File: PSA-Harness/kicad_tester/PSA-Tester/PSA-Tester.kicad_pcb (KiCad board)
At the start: 4 copper layers, 100 x 100 mm, 41 parts, among them J11 U262-241N-4BV60, M1 MountingHole_3.2mm_M3_Pad_Via, M2 MountingHole_3.2mm_M3_Pad_Via, M3 MountingHole_3.2mm_M3_Pad_Via, M4 MountingHole_3.2mm_M3_Pad_Via, SW1 B3S-1000, SW2 B3S-1000, SW3 B3S-1000, U1 MCP23017T-E/SO, U10 ESP32-C3-OLED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

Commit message: change usb-c type and button
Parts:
- J11: value U262-241N-4BV60 -> TYPE-C-31-M-04
- SW1, SW2, SW3: value B3S-1000 -> B3FS-1010P; footprint 0_tester:SW_SPST_B3S-1000 -> 0_tester:SW_SPST_Omron_B3FS-101xP

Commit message: fix DRC
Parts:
- moved SW2 0.26 mm to (129.0, 113.4)
- moved SW3 0.26 mm to (129.0, 127.4)
- moved SW1 0.26 mm to (129.0, 99.7)
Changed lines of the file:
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@@
 	(footprint "0_tester:SW_SPST_Omron_B3FS-101xP"
 		(layer "F.Cu")
-		(at 128.74 99.75 180)
+		(at 128.975 99.65 180)
 		(descr "Surface Mount Tactile Switch for High-Density Mounting, 4.3mm height, https://omronfs.omron.com/en_US/ecb/products/pdf/en-b3fs.pdf")
 		(tags "Tactile Switch")
@@
 	(footprint "0_tester:SW_SPST_Omron_B3FS-101xP"
 		(layer "F.Cu")
-		(at 128.765 127.5 180)
+		(at 129 127.4 180)
 		(descr "Surface Mount Tactile Switch for High-Density Mounting, 4.3mm height, https://omronfs.omron.com/en_US/ecb/products/pdf/en-b3fs.pdf")
 		(tags "Tactile Switch")
@@
 	(footprint "0_tester:SW_SPST_Omron_B3FS-101xP"
 		(layer "F.Cu")
-		(at 128.765 113.5 180)
+		(at 129 113.4 180)
 		(descr "Surface Mount Tactile Switch for High-Density Mounting, 4.3mm height, https://omronfs.omron.com/en_US/ecb/products/pdf/en-b3fs.pdf")
 		(tags "Tactile Switch")
@@
 	)
 	(segment
-		(start 124.79 115.75)
-		(end 125.8267 115.75)
-		(width 0.2)
-		(layer "F.Cu")
-		(net 145)
-	)
-	(segment
-		(start 130.55 129.558)
-		(end 131.5113 129.558)
+		(start 114.9466 81.5534)
+		(end 114.9 81.6)
 		(width 0.2)
 		(layer "F.Cu")
@@
 	)
 	(segment
-		(start 114.9466 81.5534)
-		(end 114.9 81.6)
+		(start 100.4059 107.5059)
+		(end 99.695 106.795)
 		(width 0.2)
 		(layer "F.Cu")
@@
 	)
 	(segment
-		(start 100.4059 107.5059)
-		(end 99.695 106.795)
+		(start 124.932 115.608)
+		(end 126.6 115.608)
 		(width 0.2)
 		(layer "F.Cu")
@@
 	)
 	(segment
-		(start 124.765 103.048)
-		(end 124.765 102)
-		(width 0.2)
-		(layer "F.Cu")
-		(net 145)
-	)
-	(segment
 		(start 56.9777 81.9637)
 		(end 58.1513 81.9637)
@@
 	)
 	(segment
+		(start 132.59 115.6)
+		(end 131.4 115.6)
+		(width 0.2)
+		(layer "F.Cu")
+		(net 145)
+	)
+	(segment
 		(start 99.895 108.065)
 		(end 99 108.065)
@@
 	)
 	(segment
-		(start 126.2245 129.558)
-		(end 126.0187 129.558)
-		(width 0.2)
-		(layer "F.Cu")
-		(net 145)
-	)
-	(segment
-		(start 132.994 114.386)
-		(end 132.74 114.64)
+		(start 108.554 80.427)
+		(end 109.727 80.427)
 		(width 0.2)
 		(layer "F.Cu")
@@
 	)
 	(segment
-		(start 108.554 80.427)
-		(end 109.727 80.427)
+		(start 99.229 88.394)
+		(end 99 88.165)
 		(width 0.2)
 		(layer "F.Cu")
@@
 	)
 	(segment
-		(start 99.229 88.394)
-		(end 99 88.165)
+		(start 132.715 102)
+		(end 131.4 102)
 		(width 0.2)
 		(layer "F.Cu")
@@
 	)
 	(segment
-		(start 131.5113 129.558)
-		(end 131.7033 129.75)
+		(start 124.896812 129.643188)
+		(end 126.8 129.643188)
 		(width 0.2)
 		(layer "F.Cu")
@@
 	)
 	(segment
-		(start 132.74 114.64)
-		(end 132.74 115.75)
-		(width 0.2)
-		(layer "F.Cu")
-		(net 145)
-	)
-	(segment
-		(start 124.79 129.75)
-		(end 125.8267 129.75)
+		(start 124.79 115.75)
+		(end 124.932 115.608)
 		(width 0.2)
 		(layer "F.Cu")
@@
 	)
 	(segment
+		(start 132.548 129.558)
+		(end 131.4 129.558)
+		(width 0.2)
+		(layer "F.Cu")
+		(net 145)
+	)
+	(segment
 		(start 81.3845 86.2742)
 		(end 82.0053 86.895)
@@
 	)
 	(segment
-		(start 124.99 103.273)
-		(end 124.765 103.048)
+		(start 124.79 129.75)
+		(end 124.896812 129.643188)
 		(width 0.2)
 		(layer "F.Cu")
@@
 	)
 	(segment
+		(start 132.74 129.75)
+		(end 132.548 129.558)
+		(width 0.2)
+		(layer "F.Cu")
+		(net 145)
+	)
+	(segment
 		(start 87.715 101.715)
 		(end 87.7 101.7)
@@
 	)
 	(segment
-		(start 126.0187 129.558)
-		(end 125.8267 129.75)
-		(width 0.2)
-		(layer "F.Cu")
-		(net 145)
-	)
-	(segment
 		(start 72.1344 100.9111)
 		(end 72.8983 101.675)
@@
 	)
 	(segment
-		(start 125.9687 115.608)
-		(end 125.8267 115.75)
-		(width 0.2)
-		(layer "F.Cu")
-		(net 145)
-	)
-	(segment
 		(start 100.4059 107.562)
 		(end 100.4059 107.5059)
@@
 	)
 	(segment
-		(start 132.74 129.75)
-		(end 131.7033 129.75)
-		(width 0.2)
-		(layer "F.Cu")
-		(net 145)
-	)
-	(segment
 		(start 45.01 80.6796)
 		(end 43.9546 81.735)
@@
 	)
 	(segment
+		(start 124.765 102)
+		(end 126.6 102)
+		(width 0.2)
+		(layer "F.Cu")
+		(net 145)
+	)
+	(segment
 		(start 70.44 105.54)
 		(end 70.45 105.55)
@@
 	)
 	(segment
-		(start 132.715 102.994)
-		(end 132.715 102)
-		(width 0.2)
-		(layer "F.Cu")
-		(net 145)
-	)
-	(segment
 		(start 109.727 80.427)
 		(end 110.9 81.6)
@@
 	)
 	(segment
-		(start 132.994 103.273)
-		(end 132.715 102.994)
-		(width 0.2)
-		(layer "F.Cu")
-		(net 145)
-	)
-	(segment
 		(start 56.9309 102.2612)
 		(end 56.9309 102.2591)
@@
 	)
 	(segment
-		(start 126.2245 115.608)
-		(end 125.9687 115.608)
+		(start 132.74 115.75)
+		(end 132.59 115.6)
 		(width 0.2)
 		(layer "F.Cu")
@@
 	)
 	(via
-		(at 132.994 114.386)
+		(at 131.4 115.6)
 		(size 0.5)
 		(drill 0.3)
@@
 	)
 	(via
-		(at 124.99 103.273)
+		(at 126.6 102)
 		(size 0.5)
 		(drill 0.3)
@@
 	)
 	(via
-		(at 126.2245 129.558)
+		(at 126.8 129.643188)
 		(size 0.5)
 		(drill 0.3)
@@
 	)
 	(via
-		(at 130.55 129.558)
+		(at 131.4 129.558)
 		(size 0.5)
 		(drill 0.3)
@@
 	)
 	(via
-		(at 126.2245 115.608)
+		(at 126.6 115.608)
 		(size 0.5)
 		(drill 0.3)
@@
 	)
 	(via
-		(at 132.994 103.273)
+		(at 131.4 102)
 		(size 0.5)
 		(drill 0.3)

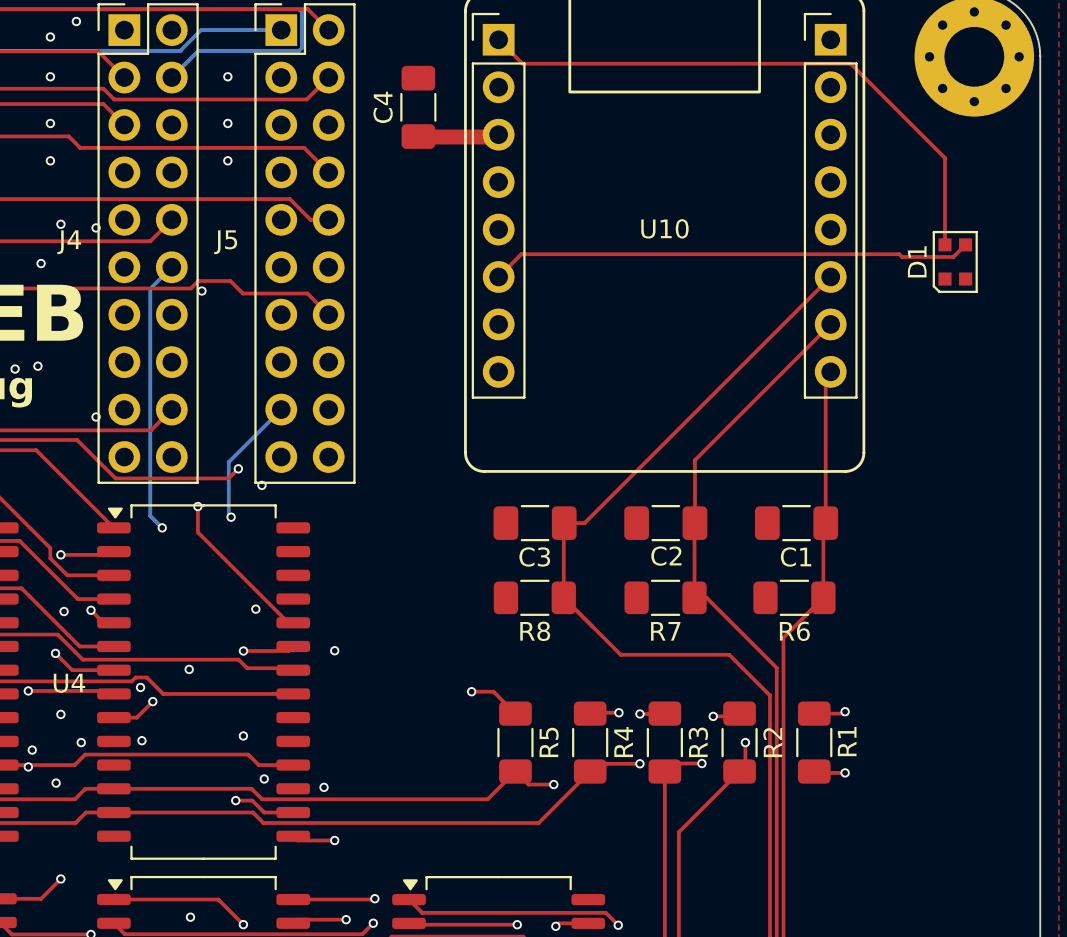
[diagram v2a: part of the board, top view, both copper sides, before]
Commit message: fix pin5/pin6 used by I2C OLED
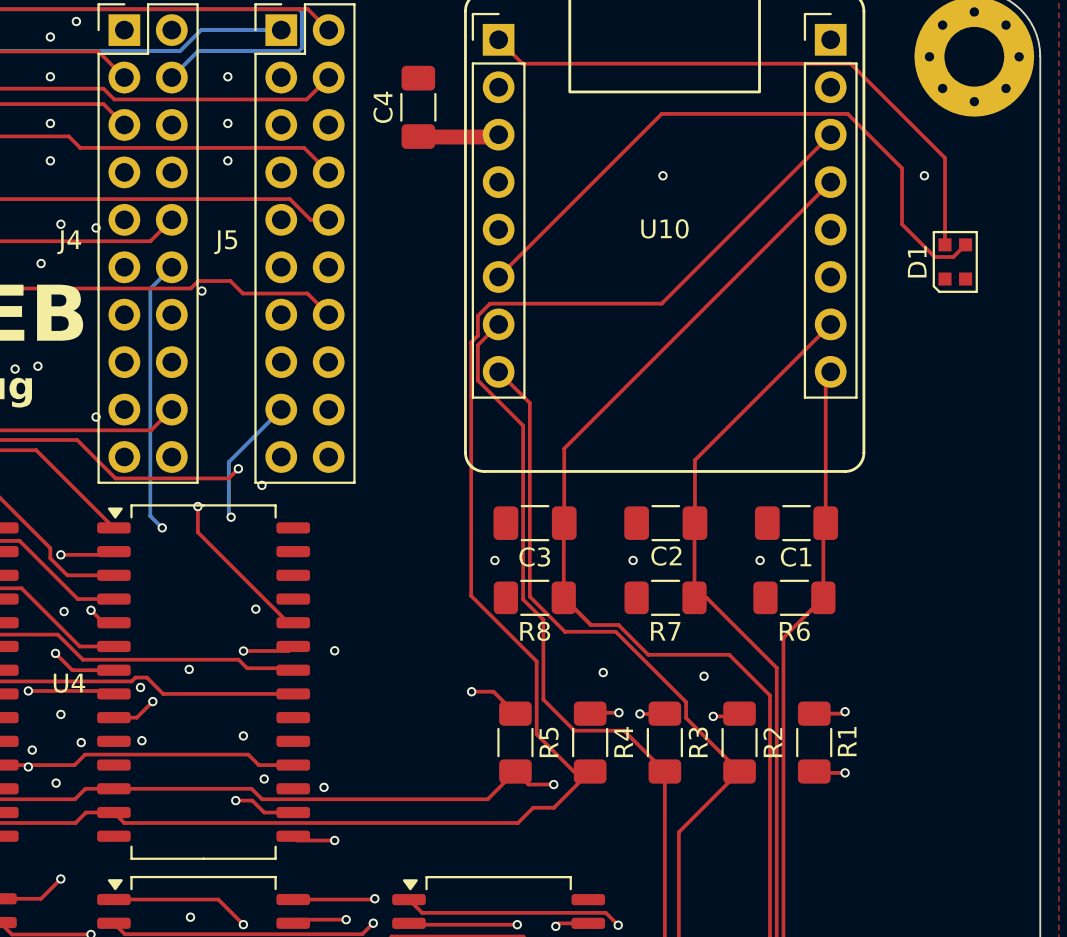
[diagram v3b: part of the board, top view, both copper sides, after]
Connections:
- U10 pad 0: unconnected-(U10-Pad0) -> SDA2
- U10 pad 1: unconnected-(U10-Pad1) -> SCL2
- U10 pad 5: BUTTON3 -> unconnected-(U10-Pad5)
- U10 pad 6: SDA2 -> unconnected-(U10-Pad6)
- U10 pad 7: SCL2 -> BUTTON3
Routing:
- net SDA1: track 186.7 -> 196.6 mm, vias 3 -> 2
- net Net-(D1-DIN): track 25.8 -> 33.8 mm
- net SCL2: track 68.4 -> 62.4 mm, vias 1 -> 0
- net BUTTON3: track 92.7 -> 97.0 mm
- net SDA2: track 66.2 -> 63.5 mm, vias 1 -> 0
- net GND: vias 58 -> 65
